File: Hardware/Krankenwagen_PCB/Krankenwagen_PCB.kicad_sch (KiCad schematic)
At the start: 14 parts, among them J1 XT60-M, J2 XT60-M, J3 XT60-M

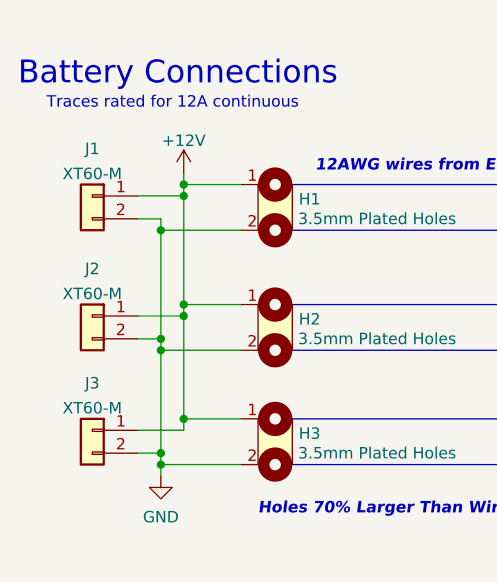
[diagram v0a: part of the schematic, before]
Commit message: Generated step file of PCB
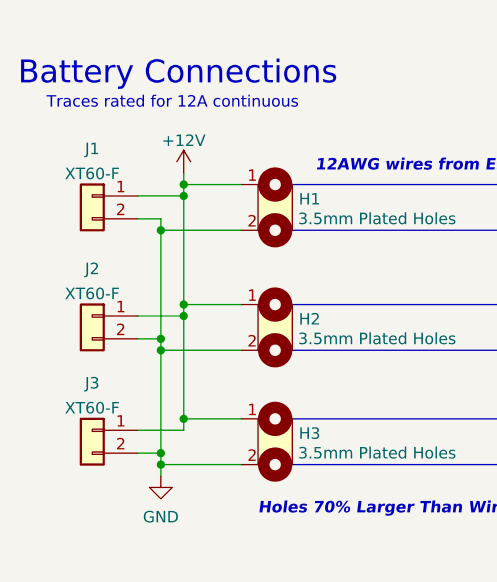
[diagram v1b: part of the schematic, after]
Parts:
- J1, J2, J3: value XT60-M -> XT60-F
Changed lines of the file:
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@@
     (in_bom yes) (on_board yes) (fields_autoplaced)
     (property "Reference" "J1" (id 0) (at 41.275 70.9635 0))
-    (property "Value" "XT60-M" (id 1) (at 41.275 73.7386 0))
+    (property "Value" "XT60-F" (id 1) (at 41.275 73.7386 0))
     (property "Footprint" "XT_Connectors:AMASS_XT60-F_1x02_P7.20mm_Vertical" (id 2) (at 41.275 76.2 0)
       (effects (font (size 1.27 1.27)) hide)
@@
     (in_bom yes) (on_board yes) (fields_autoplaced)
     (property "Reference" "J3" (id 0) (at 41.275 96.9985 0))
-    (property "Value" "XT60-M" (id 1) (at 41.275 99.7736 0))
+    (property "Value" "XT60-F" (id 1) (at 41.275 99.7736 0))
     (property "Footprint" "XT_Connectors:AMASS_XT60-F_1x02_P7.20mm_Vertical" (id 2) (at 41.275 102.235 0)
       (effects (font (size 1.27 1.27)) hide)
@@
     (in_bom yes) (on_board yes) (fields_autoplaced)
     (property "Reference" "J2" (id 0) (at 41.275 84.2985 0))
-    (property "Value" "XT60-M" (id 1) (at 41.275 87.0736 0))
+    (property "Value" "XT60-F" (id 1) (at 41.275 87.0736 0))
     (property "Footprint" "XT_Connectors:AMASS_XT60-F_1x02_P7.20mm_Vertical" (id 2) (at 41.275 89.535 0)
       (effects (font (size 1.27 1.27)) hide)
@@
     )
     (path "/4b4dd30f-bbd6-4f62-baff-f67f8a7c9999"
-      (reference "J1") (unit 1) (value "XT60-M") (footprint "XT_Connectors:AMASS_XT60-F_1x02_P7.20mm_Vertical")
+      (reference "J1") (unit 1) (value "XT60-F") (footprint "XT_Connectors:AMASS_XT60-F_1x02_P7.20mm_Vertical")
     )
     (path "/cd1ce46c-ad9f-469d-be15-0fd244d39f2a"
-      (reference "J2") (unit 1) (value "XT60-M") (footprint "XT_Connectors:AMASS_XT60-F_1x02_P7.20mm_Vertical")
+      (reference "J2") (unit 1) (value "XT60-F") (footprint "XT_Connectors:AMASS_XT60-F_1x02_P7.20mm_Vertical")
     )
     (path "/667b122c-8bea-441c-a55d-69f96aebe66f"
-      (reference "J3") (unit 1) (value "XT60-M") (footprint "XT_Connectors:AMASS_XT60-F_1x02_P7.20mm_Vertical")
-    )
-  )
+      (reference "J3") (unit 1) (value "XT60-F") (footprint "XT_Connectors:AMASS_XT60-F_1x02_P7.20mm_Vertical")
+    )
+  )
